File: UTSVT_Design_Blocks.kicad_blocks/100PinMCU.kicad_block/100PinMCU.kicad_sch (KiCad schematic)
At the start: 25 parts, among them SW1 SW_SPDT, U1 STM32G491VET6, U8 74AHC1G32, Y1 Crystal

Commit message: dog food
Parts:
- removed C11, C41: 0.1uF, Capacitor_SMD:C_0603_1608Metric_Pad1.08x0.95mm_HandSolder, symbol Device:C
- removed FB2: FerriteBead, Inductor_SMD:L_0603_1608Metric_Pad1.05x0.95mm_HandSolder, symbol Device:FerriteBead
- removed R22: 10k, Resistor_SMD:R_0603_1608Metric_Pad0.98x0.95mm_HandSolder, symbol Device:R_US
- removed SWD1: SWD, UTSVT_Connectors:Molex_Nano-Fit_105309-xx04_1x04_P2.50mm_Vertical, symbol Connector_Generic:Conn_01x04
- removed U8: 74AHC1G32, Package_TO_SOT_SMD:SOT-23-5, symbol 74xGxx:74AHC1G32
- added C12, C13: 1uF, Capacitor_SMD:C_0603_1608Metric_Pad1.08x0.95mm_HandSolder, symbol Device:C
- added J1: Conn_02x02_Odd_Even, 878320406:CONN04_878320406_MOL, symbol Connector_Generic:Conn_02x02_Odd_Even
- added R4: 10k, Resistor_SMD:R_0603_1608Metric_Pad0.98x0.95mm_HandSolder, symbol Device:R_US
- C1, C2: footprint (none) -> Capacitor_SMD:C_0603_1608Metric_Pad1.08x0.95mm_HandSolder; P/N (none) -> 0603N270F500CT
- C3: value 4.7uF -> 10uF
- SW1: footprint UTSVT_Special:SW_CJS-1200TA -> JS102011SCQN:SWITCH_1SCQN; Mouser Part Number CJS-1200TA -> (none); P/N (none) -> JS202011JCQN
- Y1: P/N (none) -> ABM3-8.000MHZ-D2Y-T
- renumbered C40 to C14, R33 to R1, R23 to R3
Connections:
- net +3.3VA is gone; now on net +3V3A: U1.36 (VREF+)
- net +3V3: now also FB1.2, J1.1 (Pin_1)
- net +3V3A: now also FB1.1, C12.1, C13.1
- net BOOT: now also R4.2
- net GND: now also J1.3 (Pin_3), R4.1; no longer FB1.2
- net GNDA: now also C12.2, C13.2; no longer FB1.1
- net SWCLK: now also J1.4 (Pin_4)
- net SWDIO: now also J1.2 (Pin_2)
- net at SW1.2 (B): now also R3.1
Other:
- note added: "BOOT = 0 (Logic LOW) Mode: Main Flash Memory. BOOT = 1 (Logic HIGH) Mode: System Memory."
- note added: "Place as close as possible to MCU VDD pins."
- note added: "Place immediately adjacent to OSC_IN/OUT."
- note added: "Place near VDDA/VSSA pins."
- note added: "Reset"
- note added: "System"
- note added: "User"
- note removed: "SWD Connector"
- moved on the sheet: C1, C10, C14, C2, C3, C4, C5, C6, C7, C8, C9, D16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

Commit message: lakshay comments addressed
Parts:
- removed FB1: FerriteBead, Inductor_SMD:L_0603_1608Metric_Pad1.05x0.95mm_HandSolder, symbol Device:FerriteBead
- removed R3: 10k, Resistor_SMD:R_0603_1608Metric_Pad0.98x0.95mm_HandSolder, symbol Device:R_US
- U1: LSCS P/N (none) -> STM32G491VET6; Mouser Part Number (none) -> 511-STM32G491VET6
- renumbered R4 to R2
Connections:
- net +3V3A is gone; now on net 3V3: C10.1, C12.1, C13.1, C9.1, U1.36 (VREF+), U1.37 (VDDA)
- net GNDA is gone; now on net GND: C10.2, C12.2, C13.2, C9.2, U1.35 (VSSA)
- net BOOT: now also SW1.2 (B)
- net SWCLK: now also J1.2 (Pin_2); no longer J1.4 (Pin_4)
- net SWDIO: now also J1.4 (Pin_4); no longer J1.2 (Pin_2)
- net +3V3 renamed 3V3
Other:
- moved on the sheet: C1, C10, C12, C13, C14, C2, C3, C4, C5, C6, C7, C8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

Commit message: post 319 brain fried stuff
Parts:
- removed D16: D_TVS, Diode_SMD:D_SOD-323, symbol Device:D_TVS
- removed R2: 10k, Resistor_SMD:R_0603_1608Metric_Pad0.98x0.95mm_HandSolder, symbol Device:R_US
- removed SW1: SW_SPDT, JS102011SCQN:SWITCH_1SCQN, symbol Switch:SW_SPDT
- added D1: D_TVS, Diode_SMD:D_SOD-323, symbol Device:D_TVS
- added R3: 10k, Resistor_SMD:R_0603_1608Metric_Pad0.98x0.95mm_HandSolder, symbol Device:R_US
- added SW2: JS202011SCQN, SW_JS202011SCQN, symbol 6pinswitch:JS202011SCQN
- C1: LCSC P/N (none) -> C92670
- C10, C14, C4, C5, C6, C7, C8, C9: LCSC P/N (none) -> C14663; P/N C0805C104M5RACTU -> MLASH168SB7104KTNA01
- C12, C13: LCSC P/N (none) -> C15849; P/N C0805C104M5RACTU -> MLASU168SB5105KTNA01
- C2: LCSC P/N (none) -> C92670; P/N 0603N270F500CT -> 0603N270F500CT
- C3: LCSC P/N (none) -> C440198; P/N GRM219R6YA475KA73D -> GRM21BR61H106KE43K
- J1: LCSC P/N (none) -> C17492485
- R1: LCSC P/N (none) -> C25804; P/N (none) -> CRCW060310K0FKEI
- Reset1: LCSC P/N (none) -> C2886926
- U1: LCSC P/N (none) -> C3209873; LSCS P/N STM32G491VET6 -> (none); Mouser Part Number 511-STM32G491VET6 -> (none); P/N (none) -> STM32G491VET6
- Y1: LCSC P/N (none) -> C144380
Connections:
- net PA13 is gone; now on net SWDIO: U1.76 (PA13)
- net PA14 is gone; now on net SWCLK: U1.77 (PA14)
- net 3V3: now also SW2.1
- net BOOT: now also D1.2 (A2), R3.2, SW2.2
- net GND: now also D1.1 (A1), R3.1, SW2.3
- net SWCLK: now also J1.4 (Pin_4); no longer J1.2 (Pin_2)
- net SWDIO: now also J1.2 (Pin_2); no longer J1.4 (Pin_4)
- no-connect marks 0 -> 3
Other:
- moved on the sheet: C1, C10, C12, C13, C14, C2, C3, C4, C5, C6, C7, C8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

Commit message: work
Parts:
- removed U1: STM32G491VET6, LQFP_491VET6_STM, symbol utsvt_ics:STM32G491VET6
- added D2: LED, symbol Device:LED
- added R2: 1k, symbol Device:R_US
- added U2: STM32G491VET6, LQFP_491VET6_STM, symbol 100PinMCU:STM32G491VET6
- D1: LCSC P/N C2831526 -> C725495; Mouser Part Number 771-PESD15VL1BA-T/R -> 833-ESDLC5V0D3B-TP; P/N PESD15VL1BA -> ESDLC5V0D3B-TP
- SW2: symbol 6pinswitch:JS202011SCQN -> Switch:SW_Push_SPDT
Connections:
- net 3V3: now also U2.100 (VDD), U2.24 (VDD), U2.36 (VREF+), U2.37 (VDDA), U2.49 (VDD), U2.6 (VBAT), U2.64 (VDD), U2.75 (VDD)
- net BOOT: now also D2.2 (A), U2.95 (PB8-BOOT0)
- net GND: now also R2.2, U2.23 (VSS), U2.35 (VSSA), U2.48 (VSS), U2.63 (VSS), U2.74 (VSS), U2.99 (VSS)
- net PA0: now also U2.20 (PA0)
- net PA1: now also U2.21 (PA1)
- net PA10: now also U2.71 (PA10)
- net PA15: now also U2.78 (PA15)
- net PA2: now also U2.22 (PA2)
- net PA3: now also U2.25 (PA3)
- net PA4: now also U2.26 (PA4)
- net PA5: now also U2.27 (PA5)
- net PA6: now also U2.28 (PA6)
- net PA7: now also U2.29 (PA7)
- net PA8: now also U2.69 (PA8)
- net PA9: now also U2.70 (PA9)
- net PB0: now also U2.32 (PB0)
- net PB1: now also U2.33 (PB1)
- net PB10: now also U2.47 (PB10)
- net PB11: now also U2.50 (PB11)
- net PB12: now also U2.51 (PB12)
- net PB13: now also U2.52 (PB13)
- net PB14: now also U2.53 (PB14)
- net PB15: now also U2.54 (PB15)
- net PB2: now also U2.34 (PB2)
- net PB3: now also U2.90 (PB3)
- net PB4: now also U2.91 (PB4)
- net PB5: now also U2.92 (PB5)
- net PB6: now also U2.93 (PB6)
- net PB7: now also U2.94 (PB7)
- net PB9: now also U2.96 (PB9)
- net PC0: now also U2.15 (PC0)
- net PC1: now also U2.16 (PC1)
- net PC10: now also U2.79 (PC10)
- net PC11: now also U2.80 (PC11)
- net PC12: now also U2.81 (PC12)
- net PC13: now also U2.7 (PC13)
- net PC14-OSC32_OUT: now also U2.8 (PC14-OSC32_IN)
- net PC15-OSC32_OUT: now also U2.9 (PC15-OSC32_OUT)
- net PC2: now also U2.17 (PC2)
- net PC3: now also U2.18 (PC3)
- net PC4: now also U2.30 (PC4)
- net PC5: now also U2.31 (PC5)
- net PC6: now also U2.65 (PC6)
- net PC7: now also U2.66 (PC7)
- net PC8: now also U2.67 (PC8)
- net PC9: now also U2.68 (PC9)
- net PD0: now also U2.82 (PD0)
- net PD1: now also U2.83 (PD1)
- net PD10: now also U2.57 (PD10)
- net PD11: now also U2.58 (PD11)
- net PD12: now also U2.59 (PD12)
- net PD13: now also U2.60 (PD13)
- net PD14: now also U2.61 (PD14)
- net PD15: now also U2.62 (PD15)
- net PD2: now also U2.84 (PD2)
- net PD3: now also U2.85 (PD3)
- net PD4: now also U2.86 (PD4)
- net PD5: now also U2.87 (PD5)
- net PD6: now also U2.88 (PD6)
- net PD7: now also U2.89 (PD7)
- net PD8: now also U2.55 (PD8)
- net PD9: now also U2.56 (PD9)
- net PE0: now also U2.97 (PE0)
- net PE1: now also U2.98 (PE1)
- net PE11: now also U2.42 (PE11)
- net PE12: now also U2.43 (PE12)
- net PE13: now also U2.44 (PE13)
- net PE14: now also U2.45 (PE14)
- net PE15: now also U2.46 (PE15)
- net PE2: now also U2.1 (PE2)
- net PE3: now also U2.2 (PE3)
- net PE4: now also U2.3 (PE4)
- net PE5: now also U2.4 (PE5)
- net PE6: now also U2.5 (PE6)
- net PE7: now also U2.38 (PE7)
- net PE8: now also U2.39 (PE8)
- net PE9: now also U2.40 (PE9)
- net PF10: now also U2.11 (PF10)
- net PF2: now also U2.19 (PF2)
- net PF9: now also U2.10 (PF9)
- net PG10-NRST: now also U2.14 (PG10-NRST)
- net SWCLK: now also U2.77 (PA14)
- net SWDIO: now also U2.76 (PA13)
- net USB_DM: now also U2.72 (PA11)
- net USB_DP: now also U2.73 (PA12)
- net at C1.2, Y1.1: now also U2.13 (PF1-OSC_OUT)
- net at C2.2, Y1.2: now also U2.12 (PF0-OSC_IN)
- new net: D2.1 (K), R2.1
- no-connect marks 3 -> 0
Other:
- moved on the sheet: C14, D1, R1, R3, Reset1

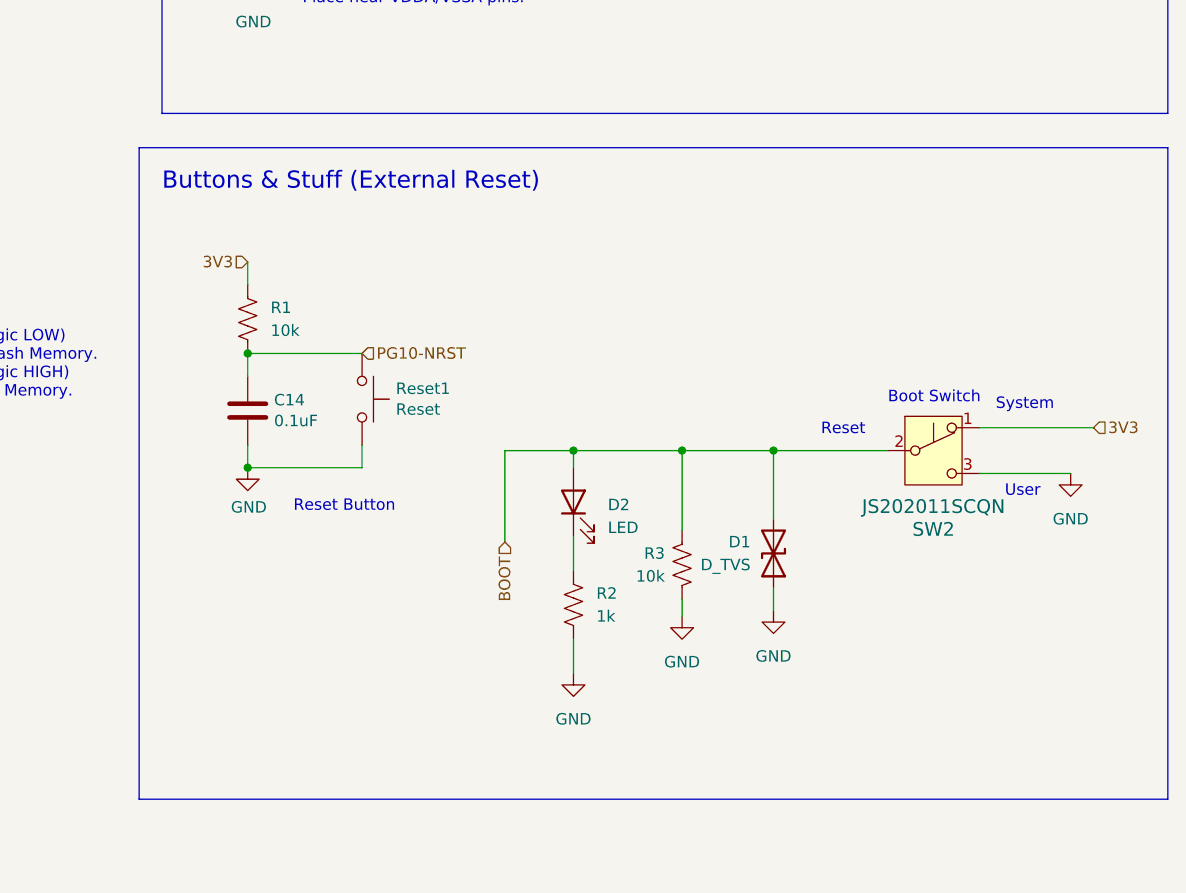
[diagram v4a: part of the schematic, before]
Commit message: updated boot sw
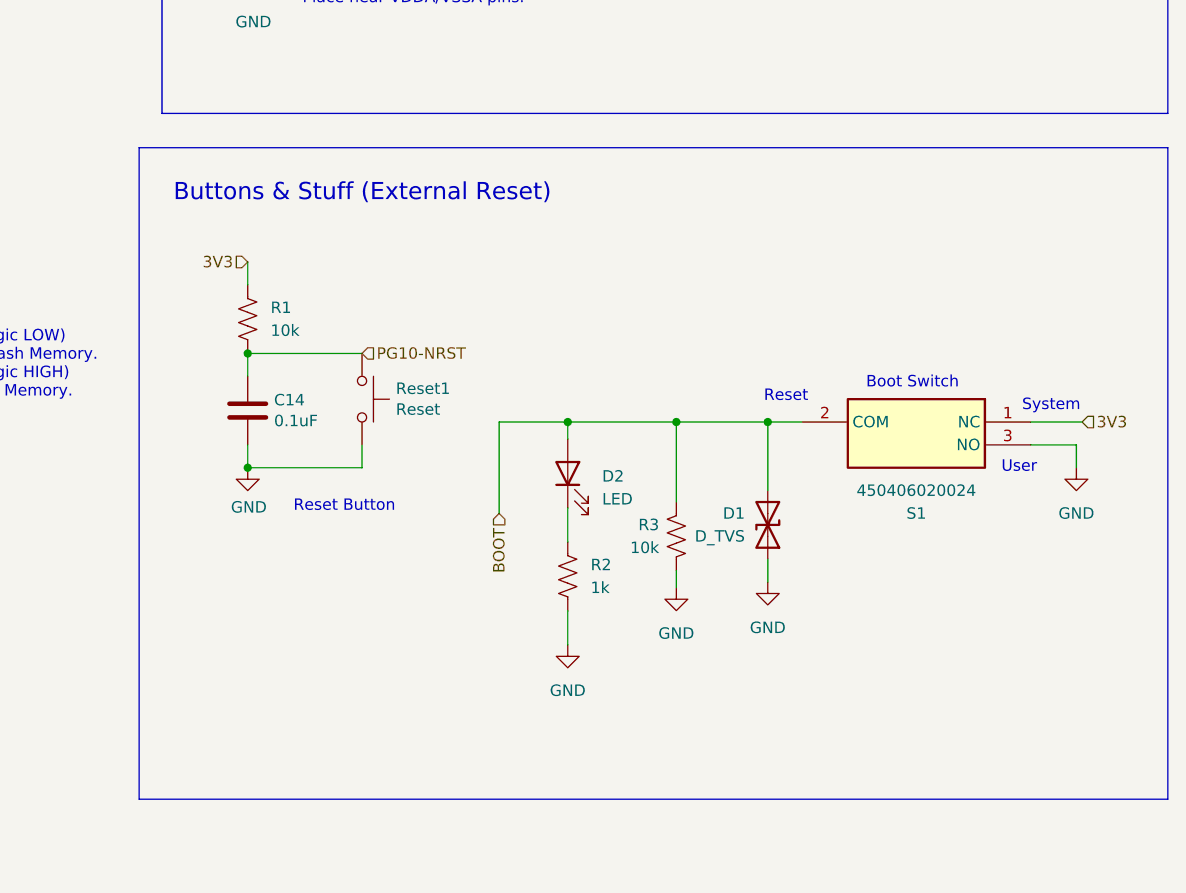
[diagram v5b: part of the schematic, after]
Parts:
- removed SW2: JS202011SCQN, SW_JS202011SCQN, symbol Switch:SW_Push_SPDT
- added S1: 450406020024, 450406020024, symbol 100PinMCU:450406020024
- U2: LCSC P/N (none) -> C3209873
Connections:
- net 3V3: now also S1.1 (NC)
- net BOOT: now also S1.2 (COM)
- net GND: now also S1.3 (NO)
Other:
- moved on the sheet: D1, D2, R2, R3
